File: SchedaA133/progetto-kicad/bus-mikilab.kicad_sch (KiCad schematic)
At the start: 6 parts, among them J1 BUS_POWER_MIKILAB, J2 BUS_MIKILAB_MAIN

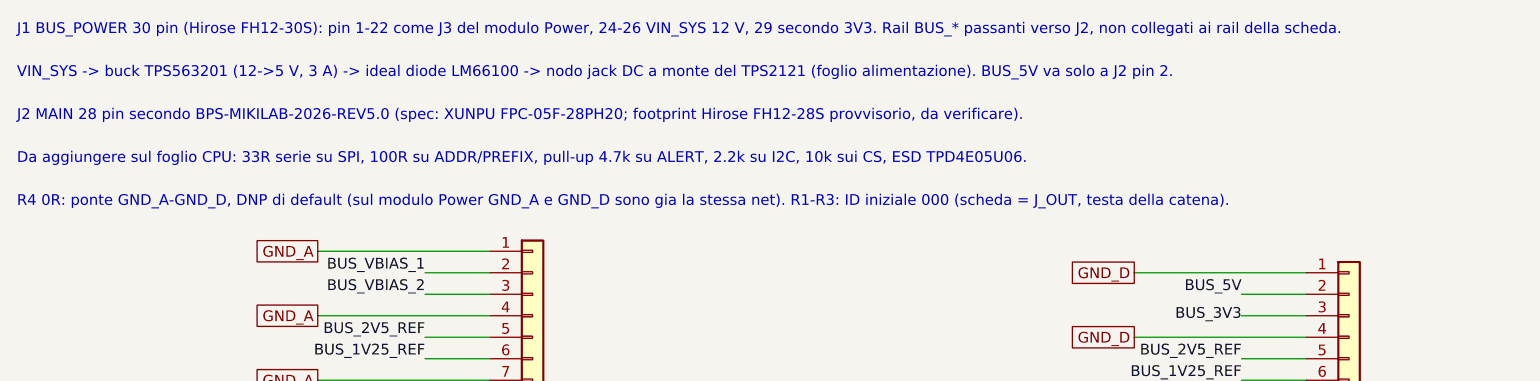
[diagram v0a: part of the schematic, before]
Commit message: SchedaA133: VREF_ENABLE attivo alto e FPC XUNPU
R324 da pull-up a pull-down 10k (VREF_ENABLE ora attivo alto sul modulo
Power). J2 MAIN con footprint XUNPU FPC-05F-28PH20 (LCSC C2856807) al
posto dell'Hirose provvisorio. Schema PDF rigenerato, ERC 0.

Co-Authored-By: Claude Opus 5.5 (1M context) <noreply@anthropic.com>
Claude-Session: https://claude.ai/code/session_01J3krgWFTUEjwvCnwUp9cQn
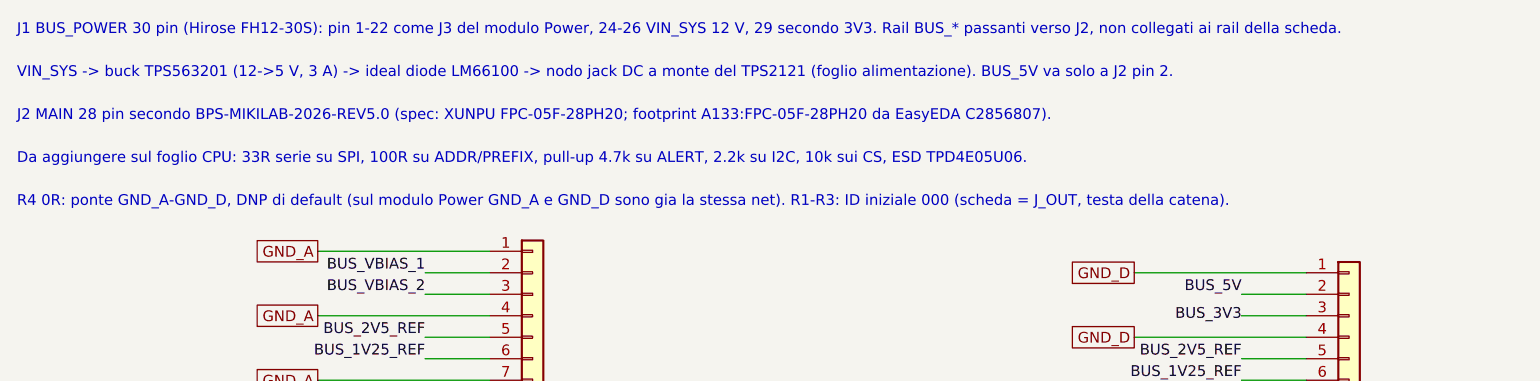
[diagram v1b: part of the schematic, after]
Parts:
- J2: footprint Connector_FFC-FPC:Hirose_FH12-28S-0.5SH_1x28-1MP_P0.50mm_Horizontal -> A133:FPC-05F-28PH20
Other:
- note added: "J2 MAIN 28 pin secondo BPS-MIKILAB-2026-REV5.0 (spec: XUNPU FPC-05F-28PH20; footprint A133:FPC-05F-28PH20 da EasyEDA C2856807)."
- note removed: "J2 MAIN 28 pin secondo BPS-MIKILAB-2026-REV5.0 (spec: XUNPU FPC-05F-28PH20; footprint Hirose FH12-28S provvisorio, da verificare)."

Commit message: Bus MIKILAB REV5.1: linea di coincidenza HIT# sul pin 28 del MAIN
Specifica: pin 28 (prima GND ridondante) = HIT#, open-drain attivo basso,
pull-up unico 4.7k sul master, impulso 100-200 ns per evento; logica di
coincidenza documentata (fronte marcato dal master, lettura dei latch).
PianoTest: HIT -> monostabile 74LVC1G123 (2k + 27 pF) -> 74LVC1G06 su
HIT#, passante J_IN -> J_OUT, ESD. ERC 0.
SchedaA133: J2 pin 28 -> PD4 (PD_EINT4), pull-up R336 4.7k, ESD su U307,
R337 0R DNP verso l'EXTINT del NEO-F10T. ERC 0, PDF rigenerato.
Documentazione bus della A133 e articolo (sezione bus e coincidenze)
aggiornati; corretta l'identita del primo piano (0).

Co-Authored-By: Claude Opus 5.5 (1M context) <noreply@anthropic.com>
Claude-Session: https://claude.ai/code/session_01J3krgWFTUEjwvCnwUp9cQn
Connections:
- net GND_D: no longer J2.28 (Pin_28)
- new net MAIN_HIT_N: J2.28 (Pin_28)
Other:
- note added: "J2 MAIN 28 pin secondo BPS-MIKILAB-2026-REV5.1 (pin 28 = HIT#) (spec: XUNPU FPC-05F-28PH20; footprint A133:FPC-05F-28PH20 da EasyEDA C2856807)."
- note removed: "J2 MAIN 28 pin secondo BPS-MIKILAB-2026-REV5.0 (spec: XUNPU FPC-05F-28PH20; footprint A133:FPC-05F-28PH20 da EasyEDA C2856807)."
